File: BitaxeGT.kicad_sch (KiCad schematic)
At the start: 14 parts

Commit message: cleaned up worksheets
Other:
- moved on the sheet: H5, H6, H7, H8

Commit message: schematic and track cleanup
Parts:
- added J1: XT30, bitaxe:XT30PW-M, symbol bitaxe:XT30PW-M
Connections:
- net 12V: now also J1.1 (+V)
- net GND: now also J1.2 (GND)
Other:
- sheet ESP32 ports: added none; removed cur_sense
- sheet Power ports: added none; removed Vsupply, cur_sense
- title: Bitaxe Gamma Turbo -> bitaxeGamma Turbo

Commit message: add new backside SMD buttons. Add new fan connector experiment (needs work)
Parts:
- H5, H6, H7, H8: footprint bitaxe:Sinhoo SMTSO3015CTJ -> bitaxe:Sinhoo SMTSO3015CTJ_nopaste
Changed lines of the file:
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@@
 			)
 		)
-		(property "Footprint" "bitaxe:Sinhoo SMTSO3015CTJ"
+		(property "Footprint" "bitaxe:Sinhoo SMTSO3015CTJ_nopaste"
 			(at 115.57 175.26 0)
 			(effects
@@
 			)
 		)
-		(property "Footprint" "bitaxe:Sinhoo SMTSO3015CTJ"
+		(property "Footprint" "bitaxe:Sinhoo SMTSO3015CTJ_nopaste"
 			(at 115.57 153.67 0)
 			(effects
@@
 			)
 		)
-		(property "Footprint" "bitaxe:Sinhoo SMTSO3015CTJ"
+		(property "Footprint" "bitaxe:Sinhoo SMTSO3015CTJ_nopaste"
 			(at 115.57 161.29 0)
 			(effects
@@
 			)
 		)
-		(property "Footprint" "bitaxe:Sinhoo SMTSO3015CTJ"
+		(property "Footprint" "bitaxe:Sinhoo SMTSO3015CTJ_nopaste"
 			(at 115.57 167.64 0)
 			(effects

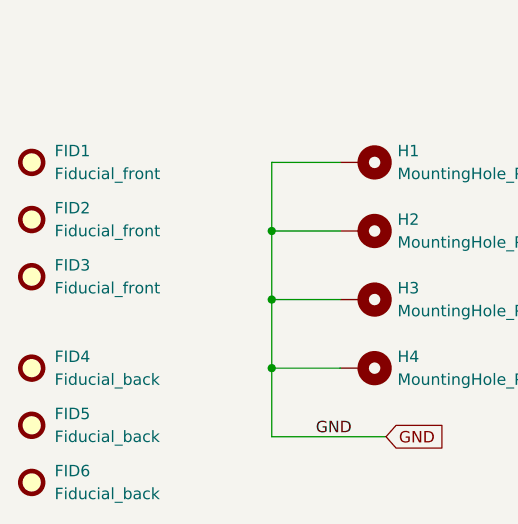
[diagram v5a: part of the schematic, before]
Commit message: cleaned up BOM and generated output. Cleaned up vias, tracks and generated gerbers
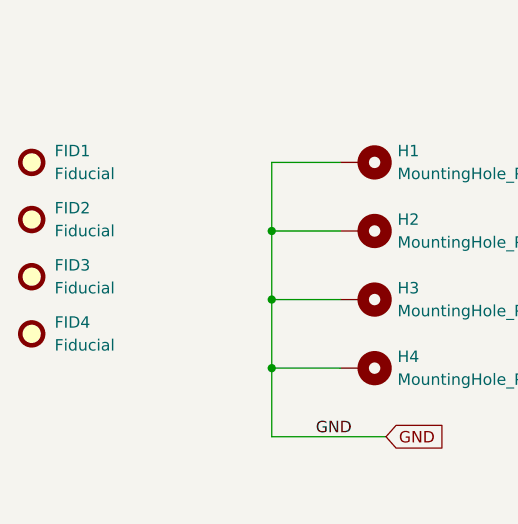
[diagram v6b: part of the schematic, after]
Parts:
- removed FID5, FID6: Fiducial_back, Fiducial:Fiducial_1mm_Mask2mm, symbol Mechanical:Fiducial
- FID1, FID2, FID3: value Fiducial_front -> Fiducial; footprint Fiducial:Fiducial_1mm_Mask2mm -> bitaxe:Fiducial_1mm_Mask2mm
- FID4: value Fiducial_back -> Fiducial; footprint Fiducial:Fiducial_1mm_Mask2mm -> bitaxe:Fiducial_1mm_Mask2mm
- J1: LCSC (none) -> C431092

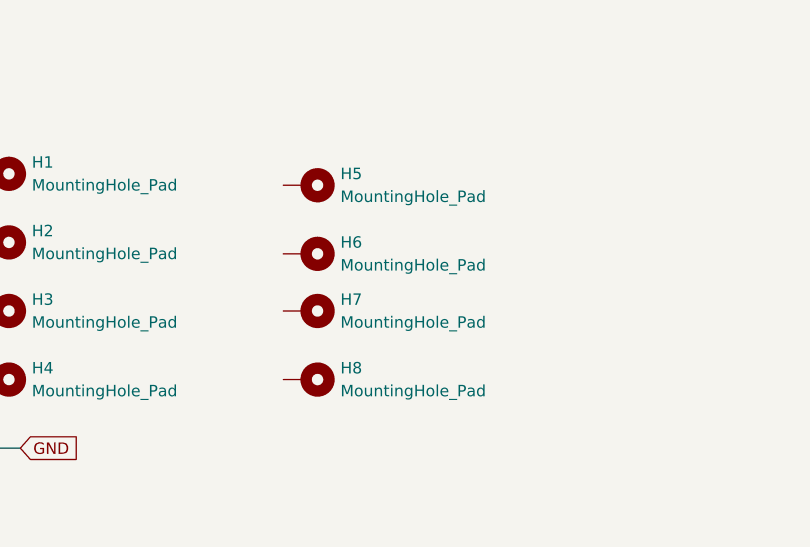
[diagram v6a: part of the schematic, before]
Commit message: add GT heatsink and single component mounting holes.
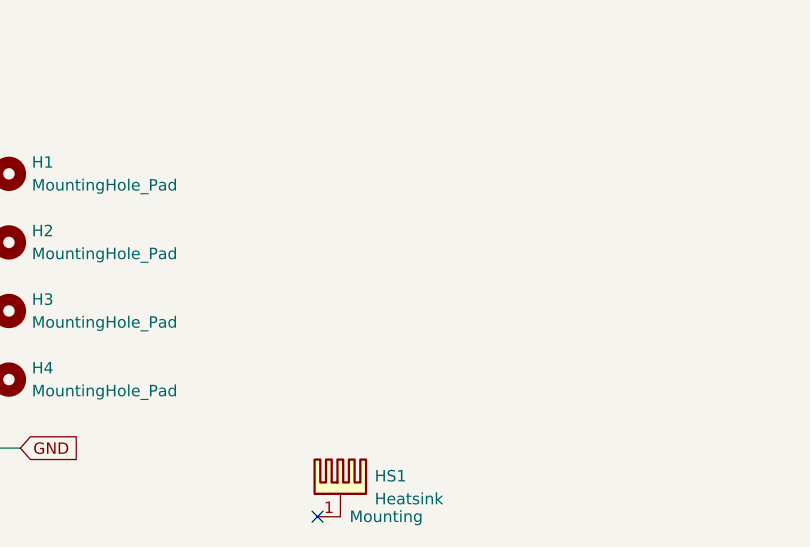
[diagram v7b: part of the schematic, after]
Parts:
- removed H5, H6, H7, H8: MountingHole_Pad, bitaxe:Sinhoo SMTSO3015CTJ_nopaste, symbol Mechanical:MountingHole_Pad
- added HS1: Heatsink, bitaxe:Heatsink-BitaxeGT, symbol bitaxe:Heatsink
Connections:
- no-connect marks 0 -> 1
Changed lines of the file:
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@@
 		(color 0 0 0 0)
+	)
+	(no_connect
+		(at 116.84 190.5)
 	)
 	(wire
@@
 	)
 	(symbol
+		(lib_id "bitaxe:Heatsink")
+		(at 119.38 187.96 0)
+		(unit 1)
+		(exclude_from_sim yes)
+		(in_bom no)
+		(on_board yes)
+		(dnp no)
+		(fields_autoplaced yes)
+		(property "Reference" "HS1"
+			(at 123.19 185.9914 0)
+			(effects
+				(font
+					(size 1.27 1.27)
+				)
+				(justify left)
+			)
+		)
+		(property "Value" "Heatsink"
+			(at 123.19 188.5314 0)
+			(effects
+				(font
+					(size 1.27 1.27)
+				)
+				(justify left)
+			)
+		)
+		(property "Footprint" "bitaxe:Heatsink-BitaxeGT"
+			(at 119.6848 187.96 0)
+			(effects
+				(font
+					(size 1.27 1.27)
+				)
+				(hide yes)
+			)
+		)
+		(property "Datasheet" "~"
+			(at 119.6848 187.96 0)
+			(effects
+				(font
+					(size 1.27 1.27)
+				)
+				(hide yes)
+			)
+		)
+		(property "Description" "Heatsink"
+			(at 119.38 187.96 0)
+			(effects
+				(font
+					(size 1.27 1.27)
+				)
+				(hide yes)
+			)
+		)
+		(pin "1"
+		)
+		(instances
+			(project ""
+				(path "/61fe8d2c-9301-4ad9-8caf-c47acfa835b0"
+					(reference "HS1")
+					(unit 1)
+				)
+			)
+		)
+	)
+	(symbol
 		(lib_id "Mechanical:MountingHole_Pad")
 		(at 81.28 175.26 270)
@@
 				(path "/61fe8d2c-9301-4ad9-8caf-c47acfa835b0"
 					(reference "H4")
-					(unit 1)
-				)
-			)
-		)
-	)
-	(symbol
-		(lib_id "Mechanical:MountingHole_Pad")
-		(at 115.57 175.26 270)
-		(unit 1)
-		(exclude_from_sim yes)
-		(in_bom no)
-		(on_board yes)
-		(dnp no)
-		(fields_autoplaced yes)
-		(property "Reference" "H8"
-			(at 119.38 173.9899 90)
-			(effects
-				(font
-					(size 1.27 1.27)
-				)
-				(justify left)
-			)
-		)
-		(property "Value" "MountingHole_Pad"
-			(at 119.38 176.5299 90)
-			(effects
-				(font
-					(size 1.27 1.27)
-				)
-				(justify left)
-			)
-		)
-		(property "Footprint" "bitaxe:Sinhoo SMTSO3015CTJ_nopaste"
-			(at 115.57 175.26 0)
-			(effects
-				(font
-					(size 1.27 1.27)
-				)
-				(hide yes)
-			)
-		)
-		(property "Datasheet" "~"
-			(at 115.57 175.26 0)
-			(effects
-				(font
-					(size 1.27 1.27)
-				)
-				(hide yes)
-			)
-		)
-		(property "Description" "Mounting Hole with connection"
-			(at 115.57 175.26 0)
-			(effects
-				(font
-					(size 1.27 1.27)
-				)
-				(hide yes)
-			)
-		)
-		(pin "1"
-		)
-		(instances
-			(project "BitaxeGT"
-				(path "/61fe8d2c-9301-4ad9-8caf-c47acfa835b0"
-					(reference "H8")
 					(unit 1)
 				)
@@
 	)
 	(symbol
-		(lib_id "Mechanical:MountingHole_Pad")
-		(at 115.57 153.67 270)
-		(unit 1)
-		(exclude_from_sim yes)
-		(in_bom no)
-		(on_board yes)
-		(dnp no)
-		(fields_autoplaced yes)
-		(property "Reference" "H5"
-			(at 119.38 152.3999 90)
-			(effects
-				(font
-					(size 1.27 1.27)
-				)
-				(justify left)
-			)
-		)
-		(property "Value" "MountingHole_Pad"
-			(at 119.38 154.9399 90)
-			(effects
-				(font
-					(size 1.27 1.27)
-				)
-				(justify left)
-			)
-		)
-		(property "Footprint" "bitaxe:Sinhoo SMTSO3015CTJ_nopaste"
-			(at 115.57 153.67 0)
-			(effects
-				(font
-					(size 1.27 1.27)
-				)
-				(hide yes)
-			)
-		)
-		(property "Datasheet" "~"
-			(at 115.57 153.67 0)
-			(effects
-				(font
-					(size 1.27 1.27)
-				)
-				(hide yes)
-			)
-		)
-		(property "Description" "Mounting Hole with connection"
-			(at 115.57 153.67 0)
-			(effects
-				(font
-					(size 1.27 1.27)
-				)
-				(hide yes)
-			)
-		)
-		(pin "1"
-		)
-		(instances
-			(project "BitaxeGT"
-				(path "/61fe8d2c-9301-4ad9-8caf-c47acfa835b0"
-					(reference "H5")
-					(unit 1)
-				)
-			)
-		)
-	)
-	(symbol
-		(lib_id "Mechanical:MountingHole_Pad")
-		(at 115.57 161.29 270)
-		(unit 1)
-		(exclude_from_sim yes)
-		(in_bom no)
-		(on_board yes)
-		(dnp no)
-		(fields_autoplaced yes)
-		(property "Reference" "H6"
-			(at 119.38 160.0199 90)
-			(effects
-				(font
-					(size 1.27 1.27)
-				)
-				(justify left)
-			)
-		)
-		(property "Value" "MountingHole_Pad"
-			(at 119.38 162.5599 90)
-			(effects
-				(font
-					(size 1.27 1.27)
-				)
-				(justify left)
-			)
-		)
-		(property "Footprint" "bitaxe:Sinhoo SMTSO3015CTJ_nopaste"
-			(at 115.57 161.29 0)
-			(effects
-				(font
-					(size 1.27 1.27)
-				)
-				(hide yes)
-			)
-		)
-		(property "Datasheet" "~"
-			(at 115.57 161.29 0)
-			(effects
-				(font
-					(size 1.27 1.27)
-				)
-				(hide yes)
-			)
-		)
-		(property "Description" "Mounting Hole with connection"
-			(at 115.57 161.29 0)
-			(effects
-				(font
-					(size 1.27 1.27)
-				)
-				(hide yes)
-			)
-		)
-		(pin "1"
-		)
-		(instances
-			(project "BitaxeGT"
-				(path "/61fe8d2c-9301-4ad9-8caf-c47acfa835b0"
-					(reference "H6")
-					(unit 1)
-				)
-			)
-		)
-	)
-	(symbol
 		(lib_id "bitaxe:XT30PW-M")
 		(at 50.8 45.72 0)
@@
 					(unit 1)
 				)
-			)
-		)
-	)
-	(symbol
-		(lib_id "Mechanical:MountingHole_Pad")
-		(at 115.57 167.64 270)
-		(unit 1)
-		(exclude_from_sim yes)
-		(in_bom no)
-		(on_board yes)
-		(dnp no)
-		(fields_autoplaced yes)
-		(property "Reference" "H7"
-			(at 119.38 166.3699 90)
-			(effects
-				(font
-					(size 1.27 1.27)
-				)
-				(justify left)
-			)
-		)
-		(property "Value" "MountingHole_Pad"
-			(at 119.38 168.9099 90)
-			(effects
-				(font
-					(size 1.27 1.27)
-				)
-				(justify left)
-			)
-		)
-		(property "Footprint" "bitaxe:Sinhoo SMTSO3015CTJ_nopaste"
-			(at 115.57 167.64 0)
-			(effects
-				(font
-					(size 1.27 1.27)
-				)
-				(hide yes)
-			)
-		)
-		(property "Datasheet" "~"
-			(at 115.57 167.64 0)
-			(effects
-				(font
-					(size 1.27 1.27)
-				)
-				(hide yes)
-			)
-		)
-		(property "Description" "Mounting Hole with connection"
-			(at 115.57 167.64 0)
-			(effects
-				(font
-					(size 1.27 1.27)
-				)
-				(hide yes)
-			)
-		)
-		(pin "1"
-		)
-		(instances
-			(project "BitaxeGT"
-				(path "/61fe8d2c-9301-4ad9-8caf-c47acfa835b0"
-					(reference "H7")
-					(unit 1)
-				)

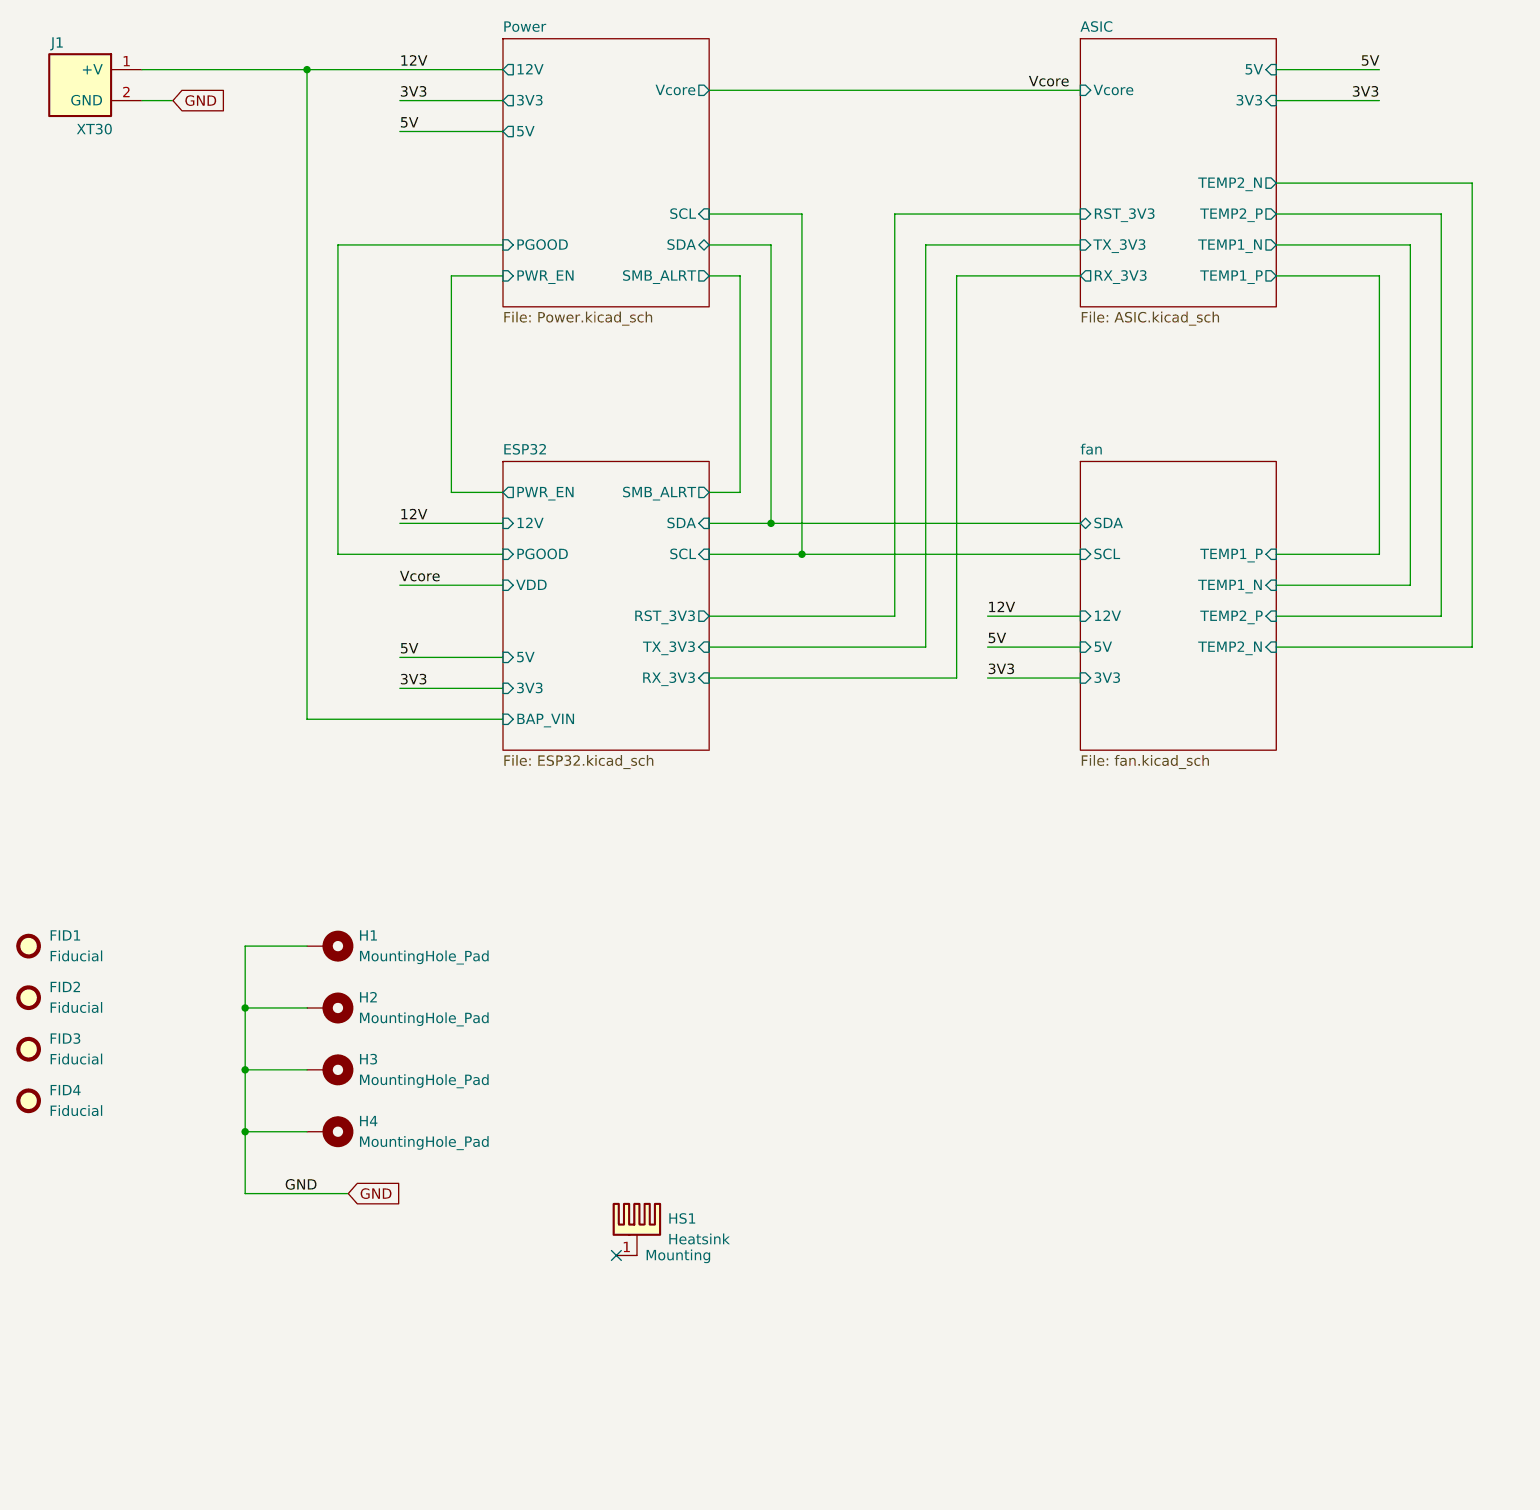
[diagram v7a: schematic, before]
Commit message: added level shifter circuit for new series-powered dual configuration. Switched TPS546D24 to single phase. I think the ASIC direction needs to be changed for proper layout
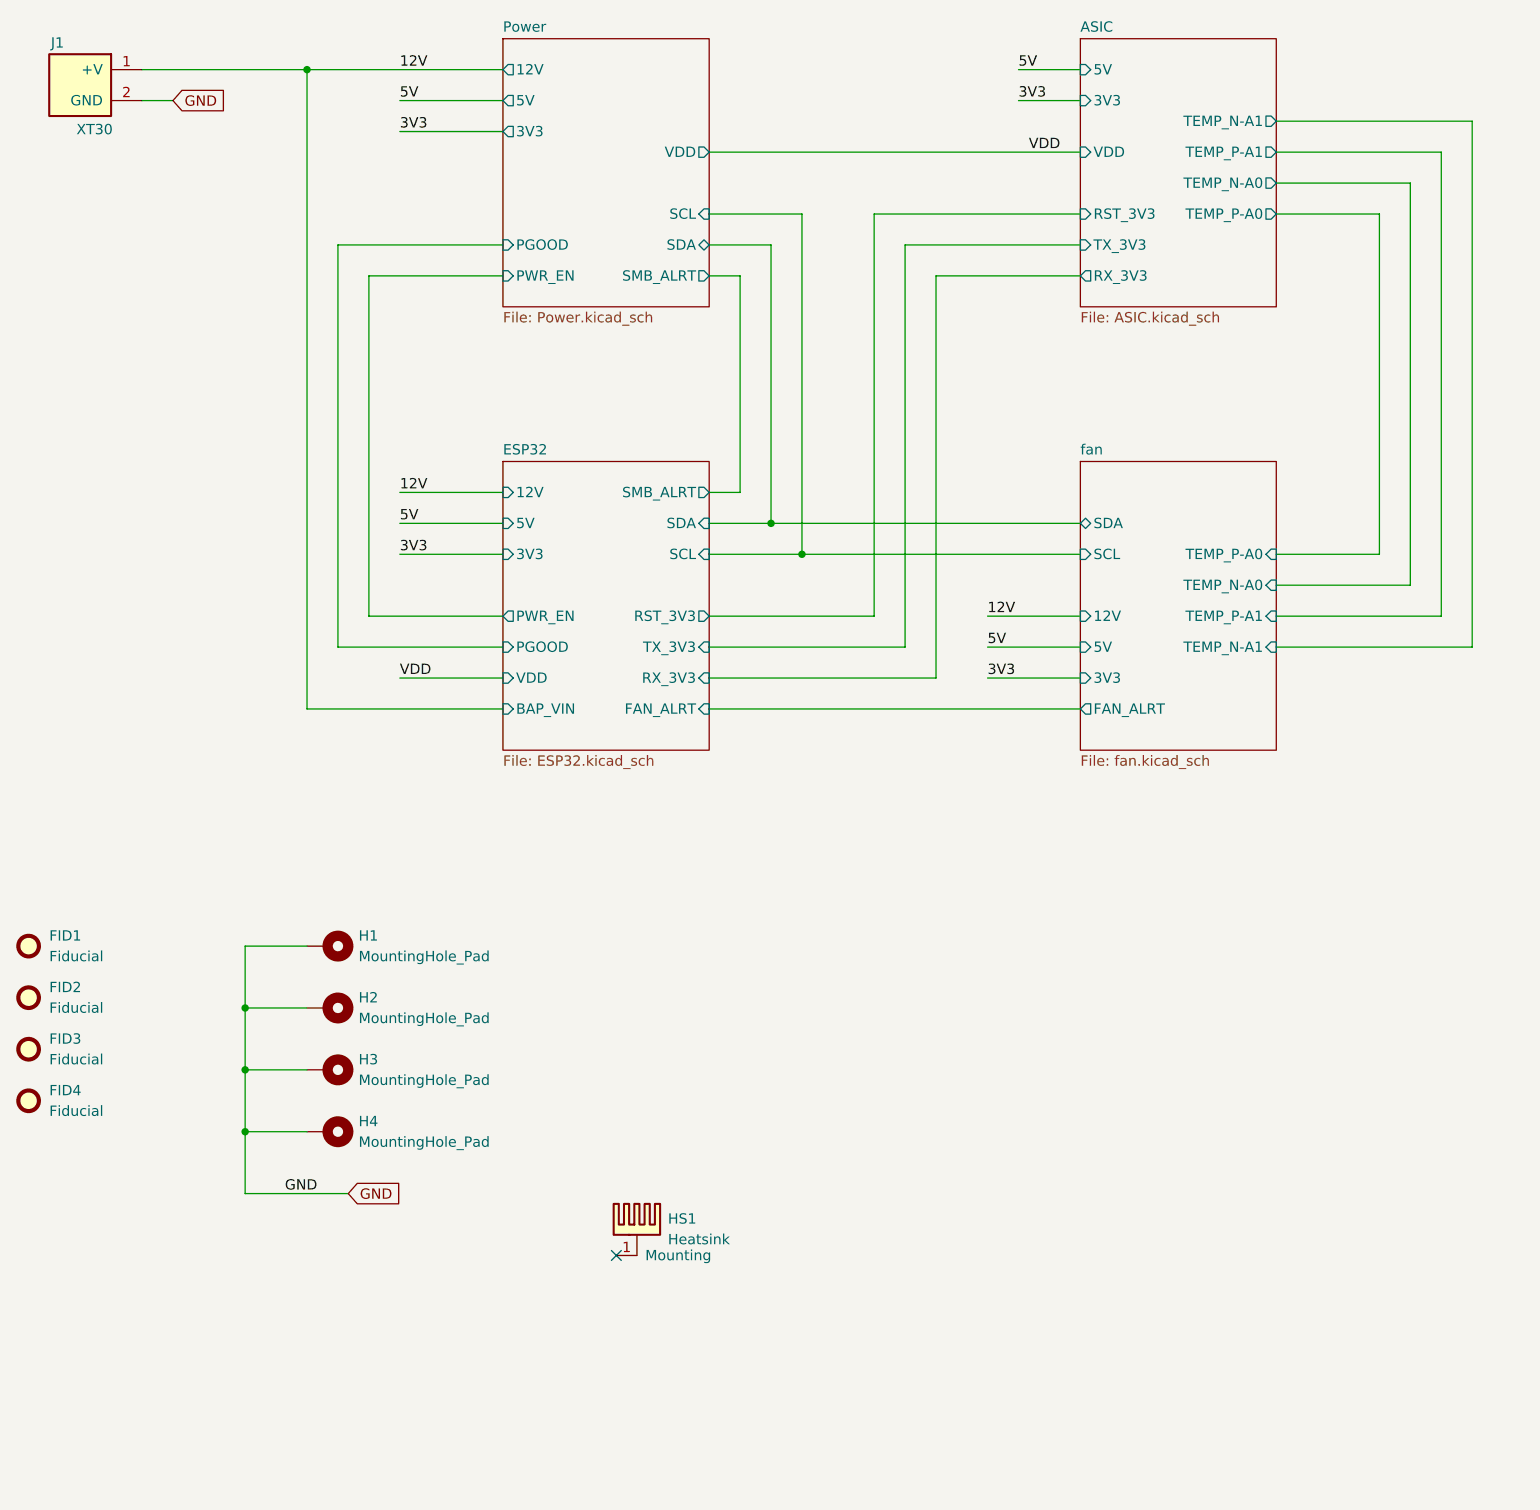
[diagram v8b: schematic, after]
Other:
- sheet ASIC ports: added TEMP_N-A0, TEMP_N-A1, TEMP_P-A0, TEMP_P-A1, VDD; removed TEMP1_N, TEMP1_P, TEMP2_N, TEMP2_P, Vcore
- sheet ESP32 ports: added FAN_ALRT; removed none
- sheet Power ports: added VDD; removed Vcore
- sheet fan ports: added FAN_ALRT, TEMP_N-A0, TEMP_N-A1, TEMP_P-A0, TEMP_P-A1; removed TEMP1_N, TEMP1_P, TEMP2_N, TEMP2_P
